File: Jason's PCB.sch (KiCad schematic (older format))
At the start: 11 parts, among them U1 Elite-C

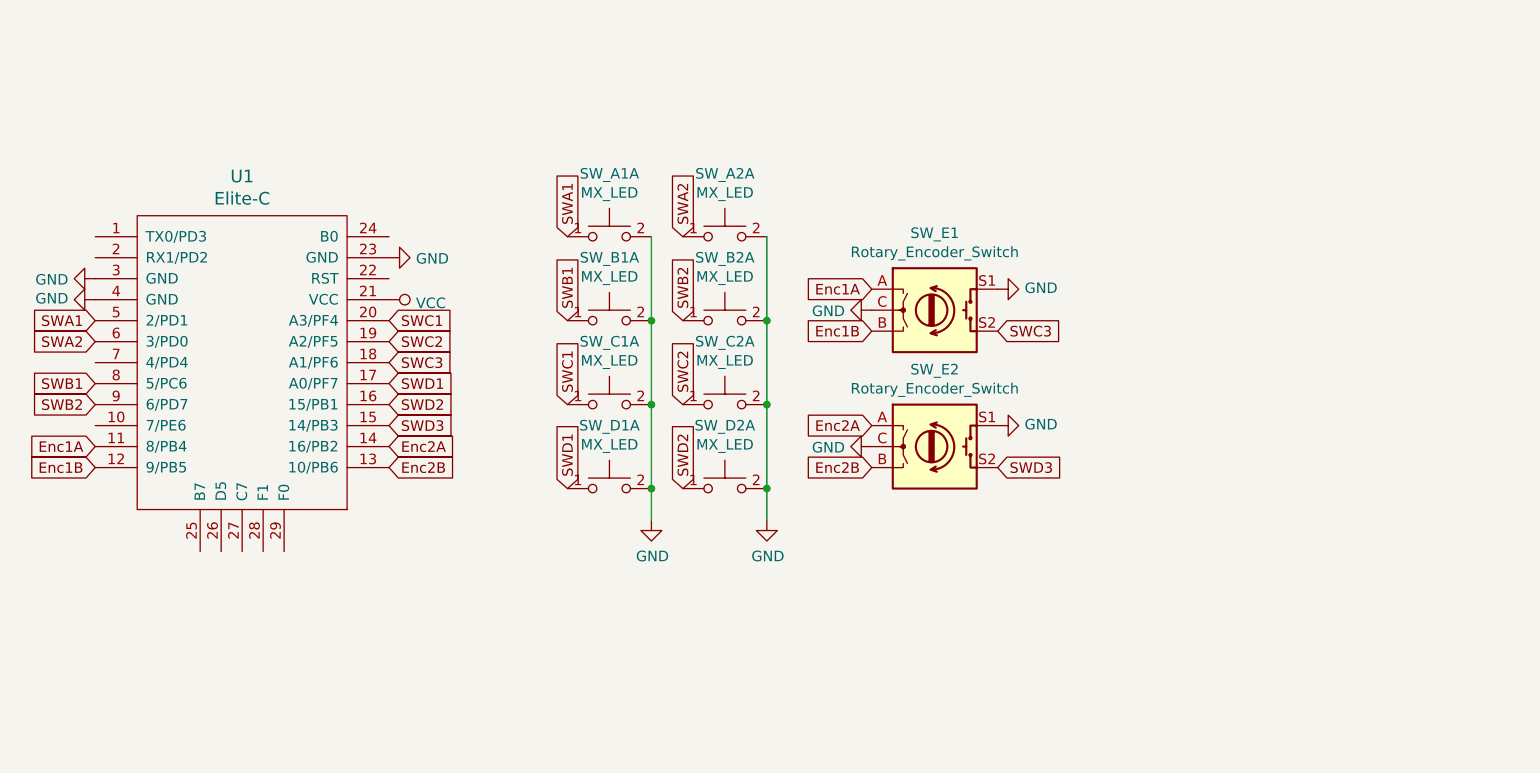
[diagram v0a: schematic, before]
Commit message: Routing
-Changed nets in schematic to make routing easier
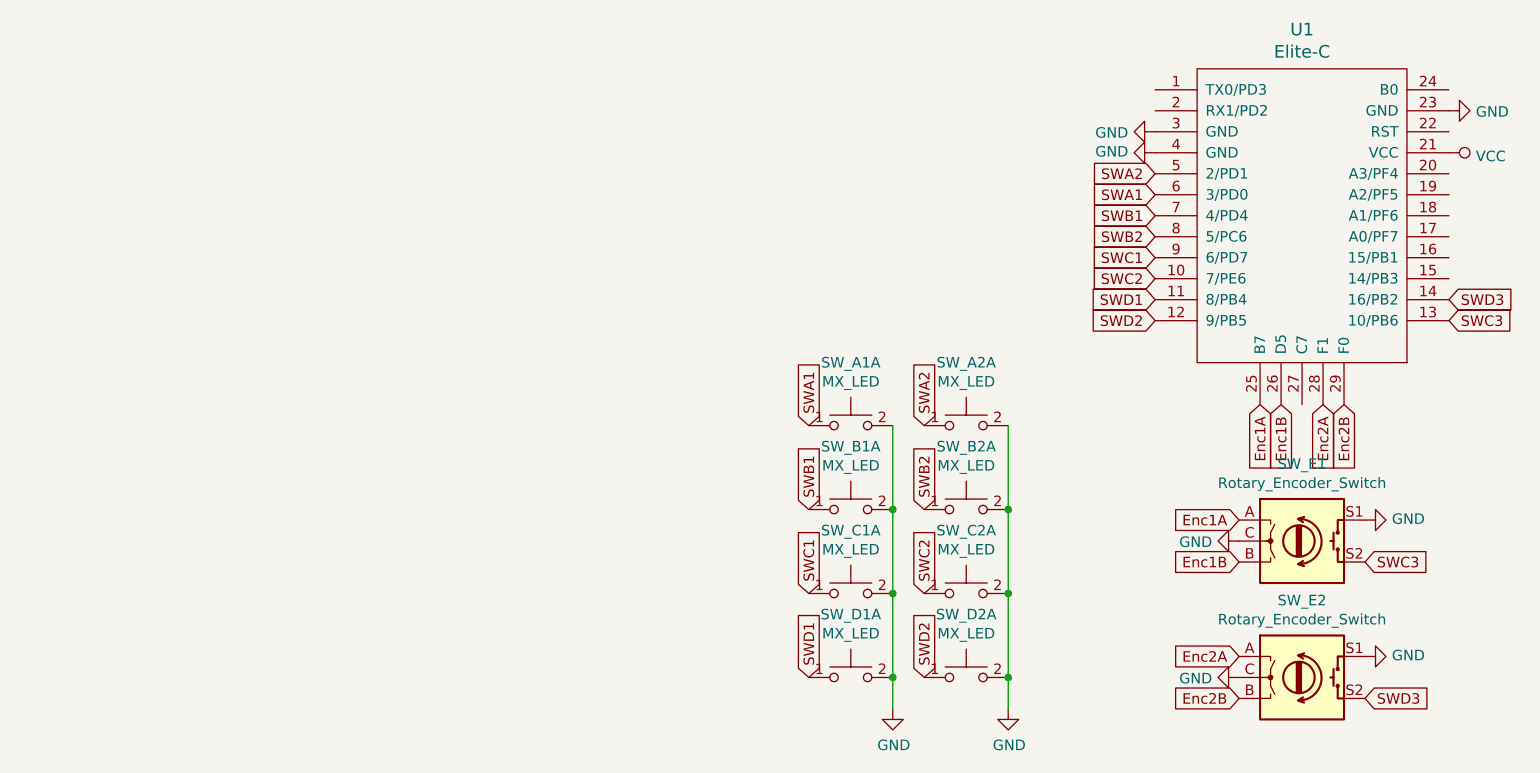
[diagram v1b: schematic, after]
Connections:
- net Enc1A: now also U1.25 (B7); no longer U1.11 (8/PB4)
- net Enc1B: now also U1.26 (D5); no longer U1.12 (9/PB5)
- net Enc2A: now also U1.28 (F1); no longer U1.14 (16/PB2)
- net Enc2B: now also U1.29 (F0); no longer U1.13 (10/PB6)
- net SWA1: now also U1.6 (3/PD0); no longer U1.5 (2/PD1)
- net SWA2: now also U1.5 (2/PD1); no longer U1.6 (3/PD0)
- net SWB1: now also U1.7 (4/PD4); no longer U1.8 (5/PC6)
- net SWB2: now also U1.8 (5/PC6); no longer U1.9 (6/PD7)
- net SWC1: now also U1.9 (6/PD7); no longer U1.20 (A3/PF4)
- net SWC2: now also U1.10 (7/PE6); no longer U1.19 (A2/PF5)
- net SWC3: now also U1.13 (10/PB6); no longer U1.18 (A1/PF6)
- net SWD1: now also U1.11 (8/PB4); no longer U1.17 (A0/PF7)
- net SWD2: now also U1.12 (9/PB5); no longer U1.16 (15/PB1)
- net SWD3: now also U1.14 (16/PB2); no longer U1.15 (14/PB3)
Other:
- moved on the sheet: SW_A1A, SW_A2A, SW_B1A, SW_B2A, SW_C1A, SW_C2A, SW_D1A, SW_D2A, SW_E1, SW_E2, U1
